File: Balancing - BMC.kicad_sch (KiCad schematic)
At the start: 15 parts, among them U3 BQ7693006DBTR

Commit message: worked on MCU
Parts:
- renumbered C49 to C11, C50 to C12, C51 to C13, C52 to C14, C54 to C15, D48 to D18, D49 to D19, D50 to D20, R136 to R36, R137 to R37, R143 to R38, R144 to R39, R145 to R40, R146 to R41, U3 to U1
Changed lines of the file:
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@@
 		(on_board yes)
 		(dnp no)
-		(property "Reference" "R144"
+		(property "Reference" "R39"
 			(at 176.276 119.634 0)
 			(effects
@@
 			(project "Project-Star"
 				(path "/fc8533bc-25dd-4c20-9b4c-ffebebd6739b/e8da5d81-614b-4fe5-84b3-4c351fab7114/630f7375-f278-4dbb-a8b3-ba91b4ac5d22"
-					(reference "R144")
+					(reference "R39")
 					(unit 1)
 				)
@@
 		(on_board yes)
 		(dnp no)
-		(property "Reference" "C51"
+		(property "Reference" "C13"
 			(at 135.89 124.714 90)
 			(effects
@@
 			(project "Project-Star"
 				(path "/fc8533bc-25dd-4c20-9b4c-ffebebd6739b/e8da5d81-614b-4fe5-84b3-4c351fab7114/630f7375-f278-4dbb-a8b3-ba91b4ac5d22"
-					(reference "C51")
+					(reference "C13")
 					(unit 1)
 				)
@@
 		(on_board yes)
 		(dnp no)
-		(property "Reference" "C52"
+		(property "Reference" "C14"
 			(at 135.89 129.794 90)
 			(effects
@@
 			(project "Project-Star"
 				(path "/fc8533bc-25dd-4c20-9b4c-ffebebd6739b/e8da5d81-614b-4fe5-84b3-4c351fab7114/630f7375-f278-4dbb-a8b3-ba91b4ac5d22"
-					(reference "C52")
+					(reference "C14")
 					(unit 1)
 				)
@@
 		(on_board yes)
 		(dnp no)
-		(property "Reference" "U3"
+		(property "Reference" "U1"
 			(at 142.24 57.15 0)
 			(effects
@@
 			(project "Project-Star"
 				(path "/fc8533bc-25dd-4c20-9b4c-ffebebd6739b/e8da5d81-614b-4fe5-84b3-4c351fab7114/630f7375-f278-4dbb-a8b3-ba91b4ac5d22"
-					(reference "U3")
+					(reference "U1")
 					(unit 1)
 				)
@@
 		(on_board yes)
 		(dnp no)
-		(property "Reference" "#PWR058"
+		(property "Reference" "#PWR03"
 			(at 173.99 115.57 0)
 			(effects
@@
 			(project "Project-Star"
 				(path "/fc8533bc-25dd-4c20-9b4c-ffebebd6739b/e8da5d81-614b-4fe5-84b3-4c351fab7114/630f7375-f278-4dbb-a8b3-ba91b4ac5d22"
-					(reference "#PWR058")
+					(reference "#PWR03")
 					(unit 1)
 				)
@@
 		(on_board yes)
 		(dnp no)
-		(property "Reference" "D48"
+		(property "Reference" "D18"
 			(at 178.054 101.6 90)
 			(effects
@@
 			(project "Project-Star"
 				(path "/fc8533bc-25dd-4c20-9b4c-ffebebd6739b/e8da5d81-614b-4fe5-84b3-4c351fab7114/630f7375-f278-4dbb-a8b3-ba91b4ac5d22"
-					(reference "D48")
+					(reference "D18")
 					(unit 1)
 				)
@@
 		(on_board yes)
 		(dnp no)
-		(property "Reference" "#PWR059"
+		(property "Reference" "#PWR04"
 			(at 195.58 71.12 0)
 			(effects
@@
 			(project "Project-Star"
 				(path "/fc8533bc-25dd-4c20-9b4c-ffebebd6739b/e8da5d81-614b-4fe5-84b3-4c351fab7114/630f7375-f278-4dbb-a8b3-ba91b4ac5d22"
-					(reference "#PWR059")
+					(reference "#PWR04")
 					(unit 1)
 				)
@@
 		(on_board yes)
 		(dnp no)
-		(property "Reference" "R146"
+		(property "Reference" "R41"
 			(at 174.244 76.2 90)
 			(effects
@@
 			(project "Project-Star"
 				(path "/fc8533bc-25dd-4c20-9b4c-ffebebd6739b/e8da5d81-614b-4fe5-84b3-4c351fab7114/630f7375-f278-4dbb-a8b3-ba91b4ac5d22"
-					(reference "R146")
+					(reference "R41")
 					(unit 1)
 				)
@@
 		(on_board yes)
 		(dnp no)
-		(property "Reference" "R136"
+		(property "Reference" "R36"
 			(at 116.586 119.634 0)
 			(effects
@@
 			(project "Project-Star"
 				(path "/fc8533bc-25dd-4c20-9b4c-ffebebd6739b/e8da5d81-614b-4fe5-84b3-4c351fab7114/630f7375-f278-4dbb-a8b3-ba91b4ac5d22"
-					(reference "R136")
+					(reference "R36")
 					(unit 1)
 				)
@@
 		(on_board yes)
 		(dnp no)
-		(property "Reference" "D50"
+		(property "Reference" "D20"
 			(at 185.166 120.65 90)
 			(effects
@@
 			(project "Project-Star"
 				(path "/fc8533bc-25dd-4c20-9b4c-ffebebd6739b/e8da5d81-614b-4fe5-84b3-4c351fab7114/630f7375-f278-4dbb-a8b3-ba91b4ac5d22"
-					(reference "D50")
+					(reference "D20")
 					(unit 1)
 				)
@@
 		(on_board yes)
 		(dnp no)
-		(property "Reference" "C54"
+		(property "Reference" "C15"
 			(at 177.8 67.564 90)
 			(effects
@@
 			(project "Project-Star"
 				(path "/fc8533bc-25dd-4c20-9b4c-ffebebd6739b/e8da5d81-614b-4fe5-84b3-4c351fab7114/630f7375-f278-4dbb-a8b3-ba91b4ac5d22"
-					(reference "C54")
+					(reference "C15")
 					(unit 1)
 				)
@@
 		(on_board yes)
 		(dnp no)
-		(property "Reference" "#PWR056"
+		(property "Reference" "#PWR02"
 			(at 132.08 138.43 0)
 			(effects
@@
 			(project "Project-Star"
 				(path "/fc8533bc-25dd-4c20-9b4c-ffebebd6739b/e8da5d81-614b-4fe5-84b3-4c351fab7114/630f7375-f278-4dbb-a8b3-ba91b4ac5d22"
-					(reference "#PWR056")
+					(reference "#PWR02")
 					(unit 1)
 				)
@@
 		(on_board yes)
 		(dnp no)
-		(property "Reference" "R143"
+		(property "Reference" "R38"
 			(at 176.276 91.694 0)
 			(effects
@@
 			(project "Project-Star"
 				(path "/fc8533bc-25dd-4c20-9b4c-ffebebd6739b/e8da5d81-614b-4fe5-84b3-4c351fab7114/630f7375-f278-4dbb-a8b3-ba91b4ac5d22"
-					(reference "R143")
+					(reference "R38")
 					(unit 1)
 				)
@@
 		(on_board yes)
 		(dnp no)
-		(property "Reference" "D49"
+		(property "Reference" "D19"
 			(at 185.166 102.87 90)
 			(effects
@@
 			(project "Project-Star"
 				(path "/fc8533bc-25dd-4c20-9b4c-ffebebd6739b/e8da5d81-614b-4fe5-84b3-4c351fab7114/630f7375-f278-4dbb-a8b3-ba91b4ac5d22"
-					(reference "D49")
+					(reference "D19")
 					(unit 1)
 				)
@@
 		(on_board yes)
 		(dnp no)
-		(property "Reference" "C50"
+		(property "Reference" "C12"
 			(at 135.89 119.634 90)
 			(effects
@@
 			(project "Project-Star"
 				(path "/fc8533bc-25dd-4c20-9b4c-ffebebd6739b/e8da5d81-614b-4fe5-84b3-4c351fab7114/630f7375-f278-4dbb-a8b3-ba91b4ac5d22"
-					(reference "C50")
+					(reference "C12")
 					(unit 1)
 				)
@@
 		(on_board yes)
 		(dnp no)
-		(property "Reference" "C49"
+		(property "Reference" "C11"
 			(at 135.89 114.554 90)
 			(effects
@@
 			(project "Project-Star"
 				(path "/fc8533bc-25dd-4c20-9b4c-ffebebd6739b/e8da5d81-614b-4fe5-84b3-4c351fab7114/630f7375-f278-4dbb-a8b3-ba91b4ac5d22"
-					(reference "C49")
+					(reference "C11")
 					(unit 1)
 				)
@@
 		(on_board yes)
 		(dnp no)
-		(property "Reference" "R137"
+		(property "Reference" "R37"
 			(at 122.936 119.634 0)
 			(effects
@@
 			(project "Project-Star"
 				(path "/fc8533bc-25dd-4c20-9b4c-ffebebd6739b/e8da5d81-614b-4fe5-84b3-4c351fab7114/630f7375-f278-4dbb-a8b3-ba91b4ac5d22"
-					(reference "R137")
+					(reference "R37")
 					(unit 1)
 				)
@@
 		(on_board yes)
 		(dnp no)
-		(property "Reference" "R145"
+		(property "Reference" "R40"
 			(at 174.244 72.39 90)
 			(effects
@@
 			(project "Project-Star"
 				(path "/fc8533bc-25dd-4c20-9b4c-ffebebd6739b/e8da5d81-614b-4fe5-84b3-4c351fab7114/630f7375-f278-4dbb-a8b3-ba91b4ac5d22"
-					(reference "R145")
-					(unit 1)
-				)
+					(reference "R40")
+					(unit 1)
+				)

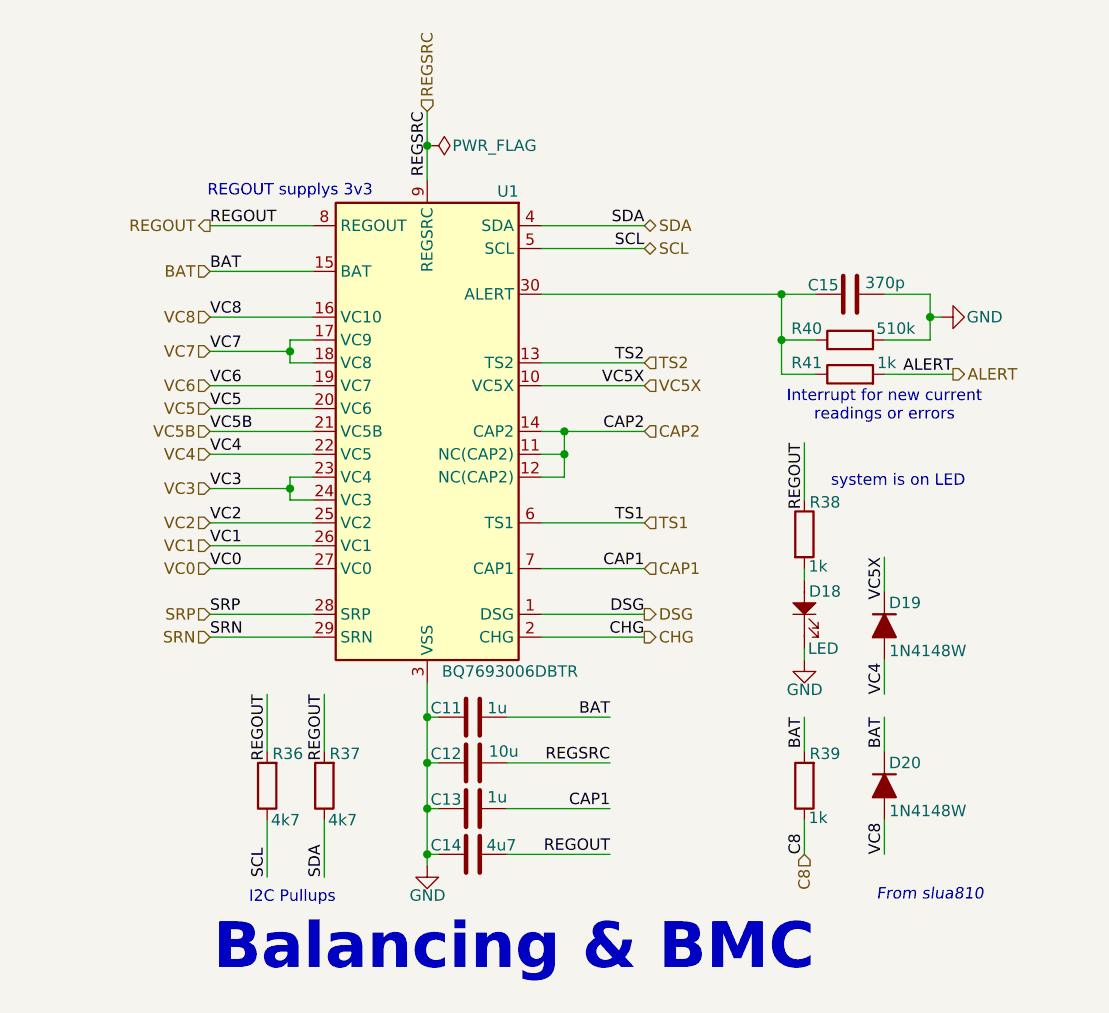
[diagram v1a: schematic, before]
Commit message: commit before simplifying and removing features
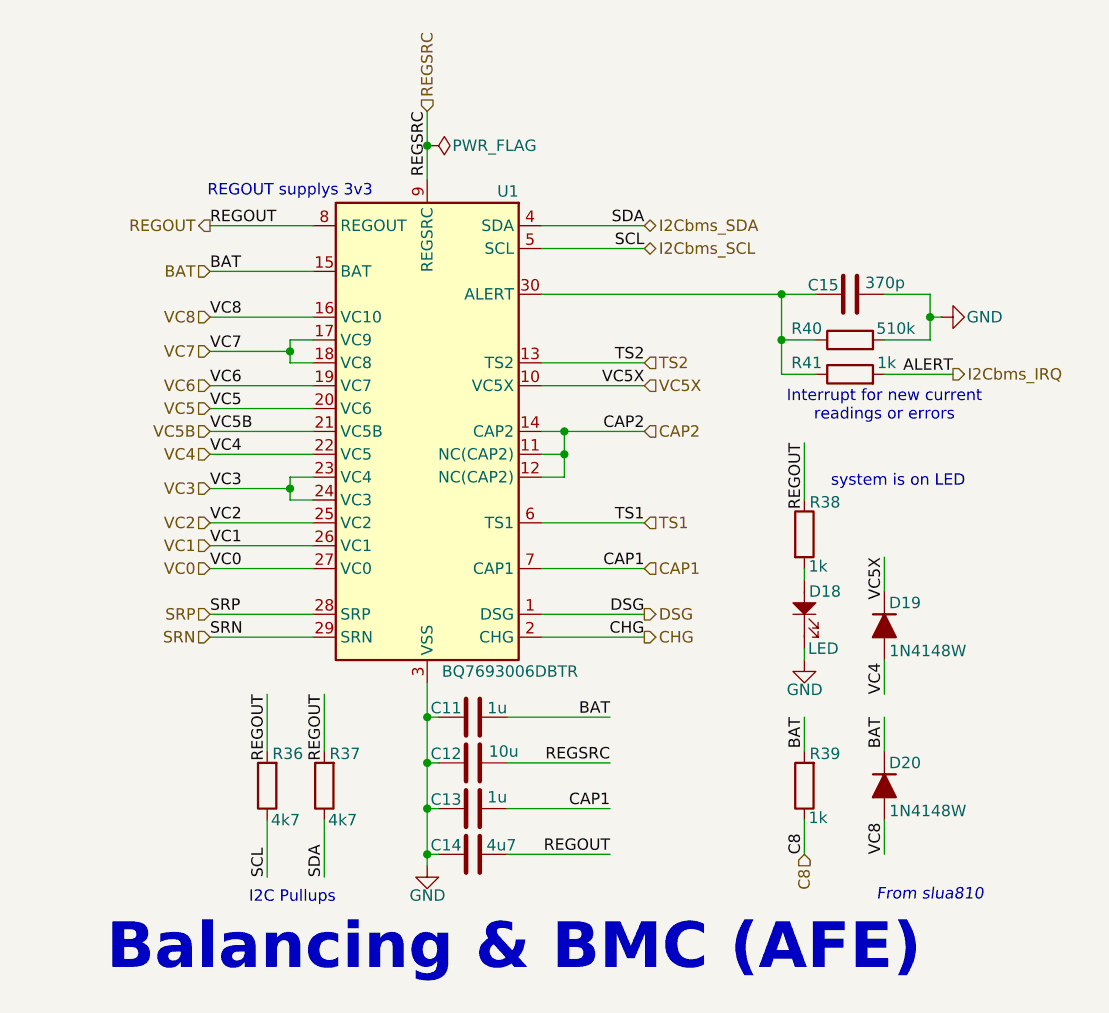
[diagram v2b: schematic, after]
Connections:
- net ALERT renamed I2Cbms_IRQ
- net SCL renamed I2Cbms_SCL
- net SDA renamed I2Cbms_SDA
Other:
- note added: "Balancing & BMC (AFE)"
- note removed: "Balancing & BMC"
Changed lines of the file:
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@@
 		)
 	)
-	(text "Balancing & BMC"
+	(text "Balancing & BMC (AFE)"
 		(exclude_from_sim no)
 		(at 141.732 141.224 0)
@@
 		)
 	)
-	(hierarchical_label "SCL"
+	(hierarchical_label "I2Cbms_SCL"
 		(shape bidirectional)
 		(at 156.21 63.5 0)
@@
 		)
 	)
-	(hierarchical_label "SDA"
+	(hierarchical_label "I2Cbms_SDA"
 		(shape bidirectional)
 		(at 156.21 60.96 0)
@@
 		)
 	)
-	(hierarchical_label "ALERT"
+	(hierarchical_label "I2Cbms_IRQ"
 		(shape output)
 		(at 190.5 77.47 0)

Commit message: Added Fuel/Gas Guage
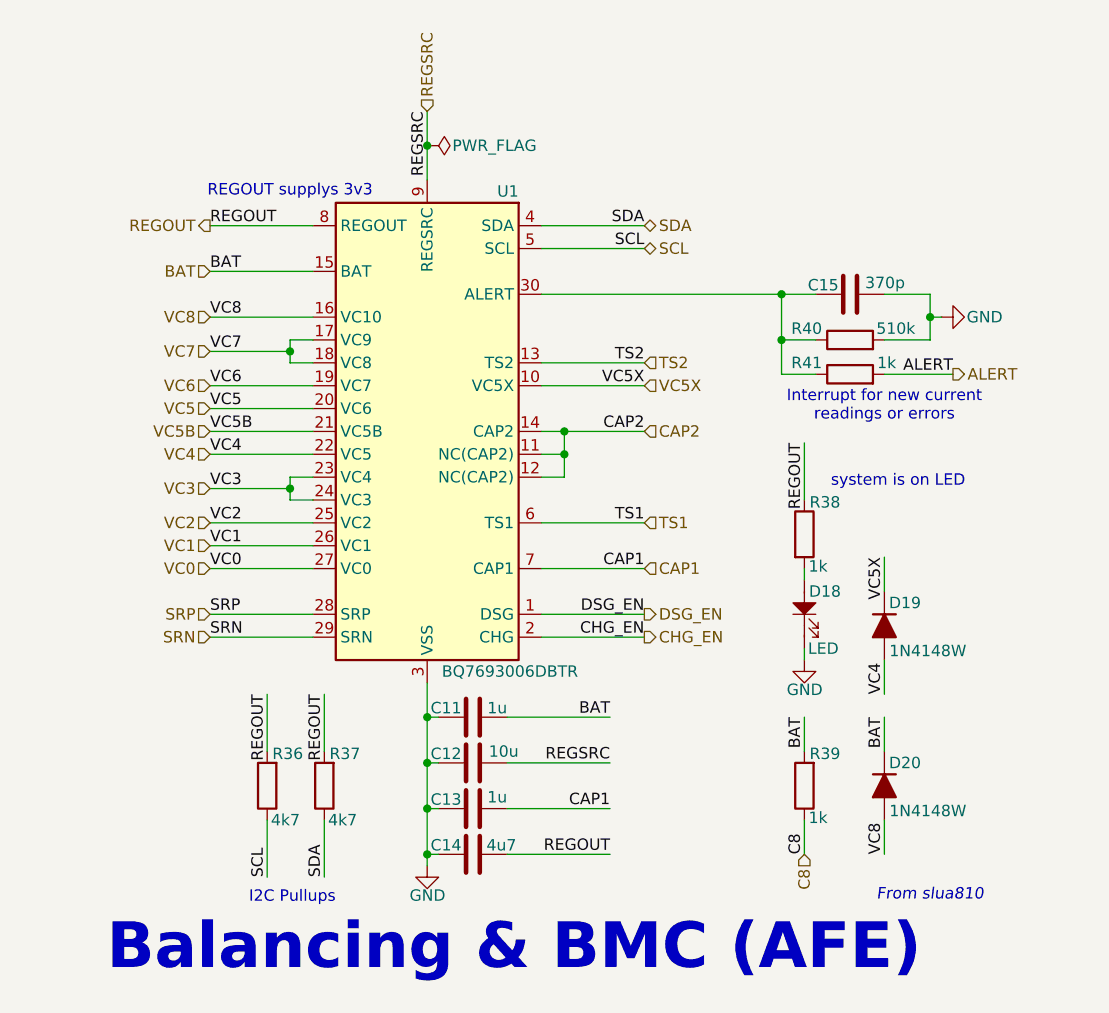
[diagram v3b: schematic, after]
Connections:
- net CHG renamed CHG_EN
- net DSG renamed DSG_EN
- net I2Cbms_IRQ renamed ALERT
- net I2Cbms_SCL renamed SCL
- net I2Cbms_SDA renamed SDA
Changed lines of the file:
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@@
 		)
 	)
-	(label "CHG"
+	(label "CHG_EN"
 		(at 156.21 106.68 180)
 		(effects
@@
 		)
 	)
-	(label "DSG"
+	(label "DSG_EN"
 		(at 156.21 104.14 180)
 		(effects
@@
 		)
 	)
-	(hierarchical_label "I2Cbms_SCL"
+	(hierarchical_label "SCL"
 		(shape bidirectional)
 		(at 156.21 63.5 0)
@@
 		)
 	)
-	(hierarchical_label "I2Cbms_SDA"
+	(hierarchical_label "SDA"
 		(shape bidirectional)
 		(at 156.21 60.96 0)
@@
 		)
 	)
-	(hierarchical_label "DSG"
+	(hierarchical_label "DSG_EN"
 		(shape output)
 		(at 156.21 104.14 0)
@@
 		)
 	)
-	(hierarchical_label "CHG"
+	(hierarchical_label "CHG_EN"
 		(shape output)
 		(at 156.21 106.68 0)
@@
 		)
 	)
-	(hierarchical_label "I2Cbms_IRQ"
+	(hierarchical_label "ALERT"
 		(shape output)
 		(at 190.5 77.47 0)
